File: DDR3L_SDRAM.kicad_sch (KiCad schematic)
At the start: 1 part, among them U2 MT41K512M8DA

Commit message: Add DDR3L nets, termination and decoupling
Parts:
- added C? (x13): C_100n_0201, antmicro-footprints:0201-res, symbol antmicroCapacitorsmisc:C_100n_0201
- added C? (x2): C_47u_0603, antmicro-footprints:0603-cap, symbol antmicroCapacitors0603:C_47u_0603
- added C? (x2): C_10u_0402, antmicro-footprints:0402-cap, symbol antmicroCapacitors0402:C_10u_0402
- added C? (x2): C_4u7_0402, antmicro-footprints:0402-cap, symbol antmicroCapacitors0402:C_4u7_0402
- added R? (x7): 4x39R_0201_array, antmicro-footprints:EXB18V, symbol antmicroResistorNetworksArrays:4x39R_0201_array
- added R?: R_100R_0201, antmicro-footprints:0201-res, symbol antmicroResistorsmisc:R_100R_0201
- added R?: R_240R_1%_0402, antmicro-footprints:0402-res, symbol antmicroResistors0402:R_240R_1%_0402
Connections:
- net VDDQ is gone; now on net +1V35: U2.B9 (VDDQ), U2.C1 (VDDQ), U2.E2 (VDDQ), U2.E9 (VDDQ)
- net VSSQ is gone; now on net GND: U2.B2 (VSSQ), U2.B8 (VSSQ), U2.C9 (VSSQ), U2.D1 (VSSQ), U2.D9 (VSSQ)
- net DDR.DQ0: now reaches U2.B3 (DQ0)
- net DDR.DM: now reaches U2.B7 (DM/TDQS)
- net DDR.DM: now also R?.7
- net DDR.DQ2: now reaches U2.C2 (DQ2)
- net DDR.DQS_P: now reaches U2.C3 (DQS)
- net DDR.DQ1: now reaches U2.C7 (DQ1)
- net DDR.DQ3: now reaches U2.C8 (DQ3)
- net DDR.DQ6: now reaches U2.D2 (NF/DQ6)
- net DDR.DQS_N: now reaches U2.D3 (DQS#)
- net +0.676_VREF: now reaches U2.E1 (VREFDQ)
- net +0.676_VREF: now also U2.J8 (VREFCA)
- net DDR.DQ4: now reaches U2.E3 (NF/DQ4)
- net DDR.DQ7: now reaches U2.E7 (NF/DQ7)
- net DDR.DQ5: now reaches U2.E8 (NF/DQ5)
- net DDR.~{RAS}: now reaches U2.F3 (RAS#)
- net DDR.~{RAS}: now also R?.7
- net DDR.CK_P: now reaches U2.F7 (CK)
- net DDR.CK_P: now also R?.2
- net DDR.ODT: now reaches U2.G1 (ODT)
- net DDR.ODT: now also R?.6
- net DDR.~{CAS}: now reaches U2.G3 (CAS#)
- net DDR.~{CAS}: now also R?.6
- net DDR.CK_N: now reaches U2.G7 (CK#)
- net DDR.CK_N: now also R?.1
- net DDR.CKE: now reaches U2.G9 (CKE)
- net DDR.CKE: now also R?.5
- net DDR.~{CS}: now reaches U2.H2 (CS#)
- net DDR.~{CS}: now also R?.8
- net DDR.~{WE}: now reaches U2.H3 (WE#)
- net DDR.~{WE}: now also R?.5
- net DDR.A10: now reaches U2.H7 (A10/AP)
- net DDR.A10: now also R?.7
- net DDR_ZQ: now reaches U2.H8 (ZQ)
- net DDR_ZQ: now also R?.2
- net DDR.BA0: now reaches U2.J2 (BA0)
- net DDR.BA0: now also R?.5
- net DDR.BA2: now reaches U2.J3 (BA2)
- net DDR.BA2: now also R?.7
- net DDR.A15: now reaches U2.J7 (A15)
- net DDR.A15: now also R?.8
- net DDR.A3: now reaches U2.K2 (A3)
- net DDR.A3: now also R?.8
- net DDR.A0: now reaches U2.K3 (A0)
- net DDR.A0: now also R?.5
- net DDR.A12: now reaches U2.K7 (A12/BC#)
- net DDR.A12: now also R?.5
- net DDR.BA1: now reaches U2.K8 (BA1)
- net DDR.BA1: now also R?.6
- net DDR.A5: now reaches U2.L2 (A5)
- net DDR.A5: now also R?.6
- net DDR.A2: now reaches U2.L3 (A2)
- net DDR.A2: now also R?.7
- net DDR.A1: now reaches U2.L7 (A1)
- net DDR.A1: now also R?.6
- net DDR.A4: now reaches U2.L8 (A4)
- net DDR.A4: now also R?.5
- net DDR.A7: now reaches U2.M2 (A7)
- net DDR.A7: now also R?.8
- net DDR.A9: now reaches U2.M3 (A9)
- net DDR.A9: now also R?.6
- net DDR.A11: now reaches U2.M7 (A11)
- net DDR.A11: now also R?.8
- net DDR.A6: now reaches U2.M8 (A6)
- net DDR.A6: now also R?.7
- net DDR.~{RESET}: now reaches U2.N2 (RESET#)
- net DDR.A13: now reaches U2.N3 (A13)
- net DDR.A13: now also R?.6
- net DDR.A14: now reaches U2.N7 (A14)
- net DDR.A14: now also R?.7
- net DDR.A8: now reaches U2.N8 (A8)
- net DDR.A8: now also R?.5
- net VDD renamed +1V35
- net +1V35: now also C?.1, C?.1, C?.1, C?.1, C?.1, C?.1, C?.1, C?.1, C?.1, C?.1, C?.1, C?.1, C?.1, C?.1
- net VSS renamed GND
- net GND: now also C?.2, C?.2, C?.2, C?.2, C?.2, C?.2, C?.2, C?.2, C?.2, C?.2, C?.2, C?.2, C?.2, C?.2, R?.1
- new net +0.676_VTT: C?.1, C?.1, C?.1, C?.1, C?.1, C?.2, C?.2, C?.2, C?.2, C?.2, R?.1, R?.1, R?.1, R?.1, R?.1, R?.1, R?.1, R?.2, R?.2, R?.2, R?.2, R?.2, R?.2, R?.2, R?.3, R?.3, R?.3, R?.3, R?.3, R?.3, R?.3, R?.4, R?.4, R?.4, R?.4, R?.4, R?.4, R?.4
- no-connect marks 0 -> 3
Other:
- note added: "DDR3L"
- note added: "DDR3L TERMINATION"
- note added: "VTT DECOUPLING"
- moved on the sheet: U2

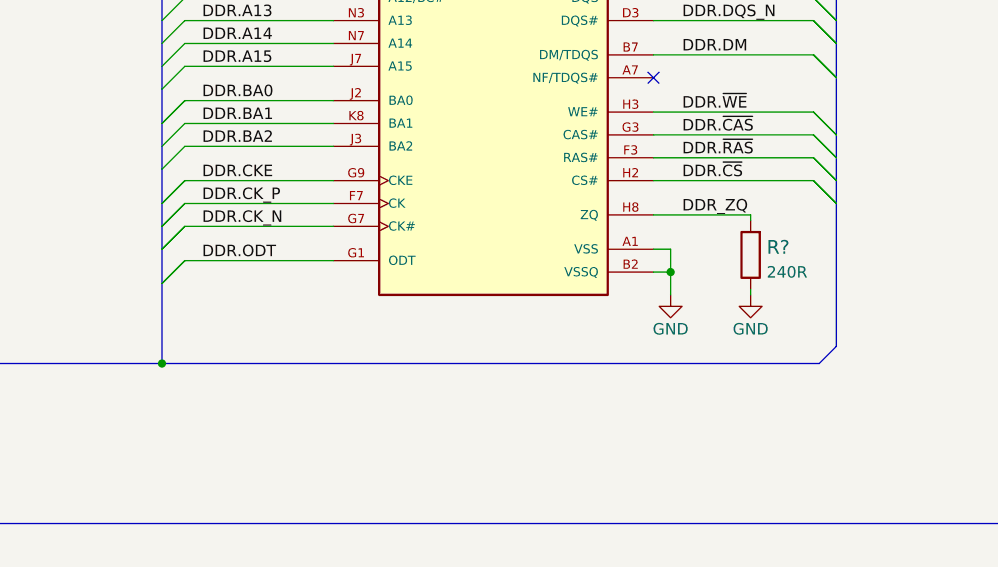
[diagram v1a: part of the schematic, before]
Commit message: Connect DDR3L to FPGA
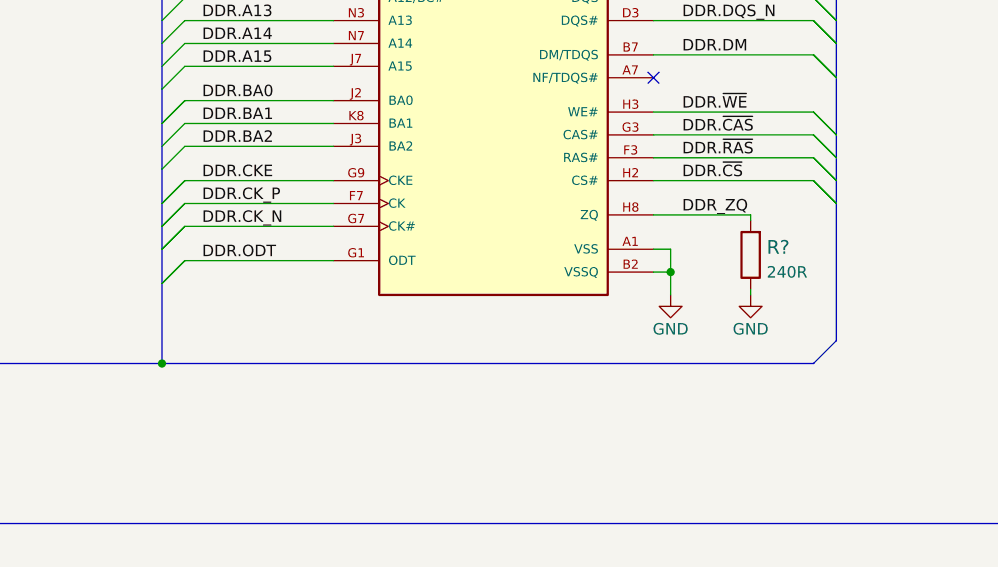
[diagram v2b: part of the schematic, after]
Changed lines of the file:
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@@
     (stroke (width 0) (type default) (color 0 0 0 0))
   )
-  (bus (pts (xy 247.65 110.49) (xy 247.65 126.365))
+  (bus (pts (xy 247.65 110.49) (xy 247.65 125.73))
     (stroke (width 0) (type default) (color 0 0 0 0))
   )
@@
     (stroke (width 0) (type default) (color 0 0 0 0))
   )
+  (bus (pts (xy 247.65 125.73) (xy 245.11 128.27))
+    (stroke (width 0) (type default) (color 0 0 0 0))
+  )
   (bus (pts (xy 230.505 197.485) (xy 230.505 209.55))
     (stroke (width 0) (type default) (color 0 0 0 0))
@@
     (stroke (width 0) (type default) (color 0 0 0 0))
   )
-  (bus (pts (xy 172.72 128.27) (xy 245.745 128.27))
+  (bus (pts (xy 172.72 128.27) (xy 245.11 128.27))
     (stroke (width 0) (type default) (color 0 0 0 0))
   )
@@
     (stroke (width 0) (type default) (color 0 0 0 0))
   )
-  (bus (pts (xy 245.745 128.27) (xy 247.65 126.365))
-    (stroke (width 0) (type default) (color 0 0 0 0))
-  )

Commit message: Add SRAM, reorganize SDRAM sheet
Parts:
- removed R? (x7): 4x39R_0201_array, antmicro-footprints:EXB18V, symbol antmicroResistorNetworksArrays:4x39R_0201_array
- added C? (x2): C_100n_0201, antmicro-footprints:0201-res, symbol antmicroCapacitorsmisc:C_100n_0201
- added C?: C_10u_0402, antmicro-footprints:0402-cap, symbol antmicroCapacitors0402:C_10u_0402
- added R? (x26): R_40R2_0201, antmicro-footprints:0201-res, symbol antmicroResistorsmisc:R_40R2_0201
- added R?: R_10k_0402, antmicro-footprints:0402-res, symbol antmicroResistors0402:R_10k_0402
- added R?: 4x39R_0201_array, antmicro-footprints:EXB18V, symbol antmicroResistorNetworksArrays:4x39R_0201_array
- added U?: AS6C8008-55ZIN, antmicro-footprints:TSOP-II-44_10.16x18.41mm_P0.8mm, symbol antmicroMemory:AS6C8008-55ZIN
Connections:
- net +0.676_VTT: now also R?.1, R?.1, R?.1, R?.1, R?.1, R?.1, R?.1, R?.1, R?.1, R?.1, R?.1, R?.1, R?.1, R?.1, R?.1, R?.1, R?.1, R?.1, R?.1, R?.1, R?.1, R?.1, R?.1, R?.1, R?.1, R?.1
- net DDR.A0: now also R?.2
- net DDR.A1: now also R?.2
- net DDR.A10: now also R?.2
- net DDR.A11: now also R?.2
- net DDR.A12: now also R?.2
- net DDR.A13: now also R?.2
- net DDR.A14: now also R?.2
- net DDR.A15: now also R?.2
- net DDR.A2: now also R?.2
- net DDR.A3: now also R?.2
- net DDR.A4: now also R?.2
- net DDR.A5: now also R?.2
- net DDR.A6: now also R?.2
- net DDR.A7: now also R?.2
- net DDR.A8: now also R?.2
- net DDR.A9: now also R?.2
- net DDR.BA0: now also R?.2
- net DDR.BA1: now also R?.2
- net DDR.BA2: now also R?.2
- net DDR.CKE: now also R?.2
- net DDR.DM: now also R?.2
- net DDR.ODT: now also R?.2
- net DDR.~{CAS}: now also R?.2
- net DDR.~{CS}: now also R?.2
- net DDR.~{RAS}: now also R?.2
- net DDR.~{RESET}: now also R?.2
- net DDR.~{WE}: now also R?.2
- net GND: now also C?.2, C?.2, C?.2, R?.1, U?.12 (VSS), U?.34 (VSS)
- new net +3V3: C?.1, C?.1, C?.1, R?.1, R?.2, R?.3, R?.4, U?.11 (VCC), U?.33 (VCC)
- new net SRAM.A0: U?.5 (A0)
- new net SRAM.A1: U?.4 (A1)
- new net SRAM.A10: U?.27 (A10)
- new net SRAM.A11: U?.26 (A11)
- new net SRAM.A12: U?.25 (A12)
- new net SRAM.A13: U?.24 (A13)
- new net SRAM.A14: U?.23 (A14)
- new net SRAM.A15: U?.22 (A15)
- new net SRAM.A16: U?.21 (A16)
- new net SRAM.A17: U?.20 (A17)
- new net SRAM.A18: U?.19 (A18)
- new net SRAM.A19: U?.18 (A19)
- new net SRAM.A2: U?.3 (A2)
- new net SRAM.A3: U?.2 (A3)
- new net SRAM.A4: U?.1 (A4)
- new net SRAM.A5: U?.44 (A5)
- new net SRAM.A6: U?.43 (A6)
- new net SRAM.A7: U?.42 (A7)
- new net SRAM.A8: U?.39 (A8)
- new net SRAM.A9: U?.28 (A9)
- new net SRAM.CE2: R?.6, U?.40 (CE2)
- new net SRAM.DQ0: U?.9 (DQ0)
- new net SRAM.DQ1: U?.10 (DQ1)
- new net SRAM.DQ2: U?.13 (DQ2)
- new net SRAM.DQ3: U?.14 (DQ3)
- new net SRAM.DQ4: U?.31 (DQ4)
- new net SRAM.DQ5: U?.32 (DQ5)
- new net SRAM.DQ6: U?.35 (DQ6)
- new net SRAM.DQ7: U?.36 (DQ7)
- new net SRAM.~{CE}: R?.5, U?.6 (CE#)
- new net SRAM.~{OE}: R?.7, U?.41 (OE#)
- new net SRAM.~{WE}: R?.8, U?.17 (WE#)
- no-connect marks 3 -> 1
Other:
- note added: "SRAM"
- note added: "Termination"
- note removed: "DDR3L TERMINATION"
- moved on the sheet: C?, R?, U2

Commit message: Unify title block
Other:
- title: (none) -> K410T devboard
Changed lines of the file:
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@@
   (paper "A3")
   (title_block
-    (comment 1 "www.antmicro.com")
-    (comment 2 "Antmicro Ltd")
+    (title "K410T devboard")
+    (date "2022-12-20")
+    (rev "0.0.99")
   )
   (junction (at 160.02 121.92) (diameter 0) (color 0 0 0 0)
